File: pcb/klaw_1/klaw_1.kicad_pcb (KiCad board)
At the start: 2 copper layers, 128.2 x 99 mm, 71 parts, among them J1 PJ-320A-4P, J3 lv27, SW1 SW_PUSH-MX_W_LED, SW10 SW_PUSH-MX_W_LED, SW12 SW_PUSH-MX_W_LED, SW13 SW_PUSH-MX_W_LED, SW14 SW_PUSH-MX_W_LED, SW15 SW_PUSH-MX_W_LED, SW16 SW_PUSH-MX_W_LED, SW18 EC11E15244G1, SW2 SW_PUSH-MX_W_LED, SW20 SW_PUSH-MX_W_LED, SW21 SW_PUSH-MX_W_LED, SW3 SW_PUSH-MX_W_LED, SW4 SW_PUSH-MX_W_LED, SW5 SW_PUSH-MX_W_LED, SW6 SW_PUSH-MX_W_LED, SW7 SW_PUSH-MX_W_LED, SW8 SW_PUSH-MX_W_LED, SW9 SW_PUSH-MX_W_LED, U1 ProMicro

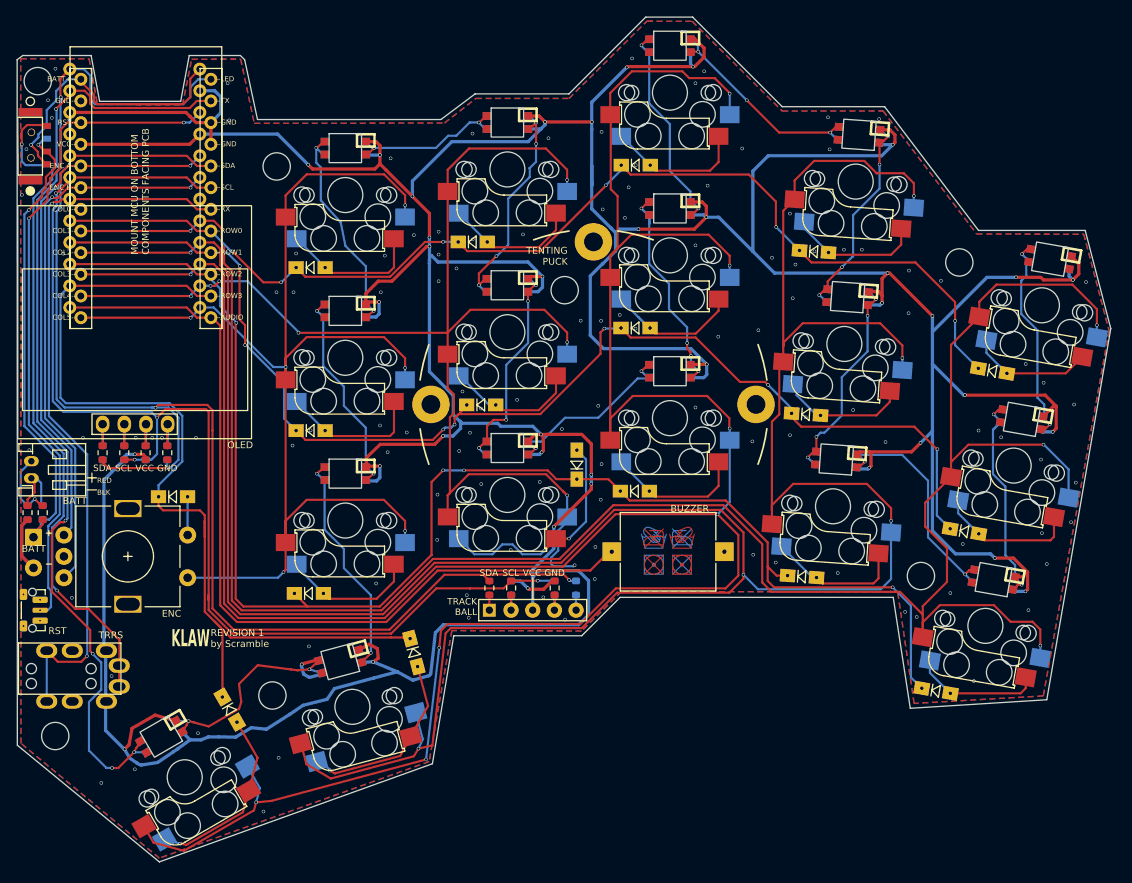
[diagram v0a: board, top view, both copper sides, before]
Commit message: feat: shorter encoder - Alps EC11N1525404
- replaces EC11E15244G1: same exact EC11 footprint, 15mm D-cut
  shaft, 19.5mm above PCB (was 24.5mm) - matches the original KLOR
  height spec; 30 det/15 pulse, 1.5mm switch travel
- official Alps 3D CAD model, baked to footprint orientation
- sourcing fields, build BOMs, and fab BOMs updated (C470748)
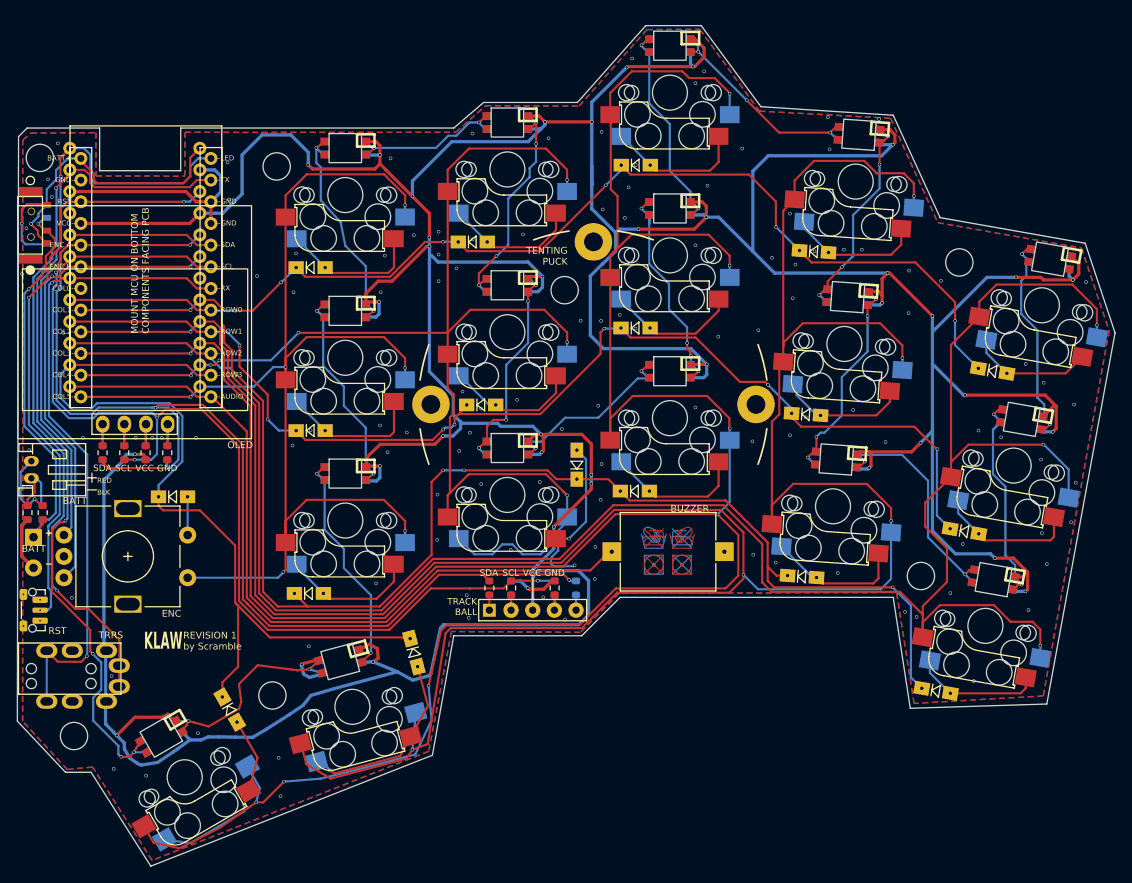
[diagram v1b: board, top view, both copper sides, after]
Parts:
- moved PSW1 9.27 mm to (82.9, 71.3)
- moved U1 9.27 mm to (97.6, 80.9)
- moved MH1 9.00 mm to (85.3, 67.2)
- moved MH6 2.20 mm to (89.3, 135.0)
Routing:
- net col3: track 331.7 -> 318.9 mm
- net SCL: track 140.1 -> 127.5 mm
- net LED: track 118.6 -> 106.1 mm
- net col2: track 328.8 -> 316.5 mm
- net SDA: track 156.6 -> 144.6 mm
- net col1: track 259.4 -> 247.8 mm
- net AUDIO: track 100.6 -> 89.0 mm
- net row3: track 111.1 -> 100.2 mm
- net row2: track 172.4 -> 161.4 mm
- net ENCB: track 65.4 -> 56.1 mm
- net RESET: track 78.3 -> 69.0 mm
- net ENCA: track 62.4 -> 53.1 mm
- net RX: track 85.9 -> 76.7 mm
- net /PSW: track 53.8 -> 44.5 mm
- net TX: track 95.8 -> 86.5 mm
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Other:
- board size 128.2 x 99 mm -> 128.6 x 98.5 mm
